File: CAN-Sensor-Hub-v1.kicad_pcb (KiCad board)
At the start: 2 copper layers, 51 x 51.5 mm, 55 parts, among them J1 Conn_01x04, J10 Conn_01x03, J2 Conn_01x04, J3 Conn_01x04, J4 USB_C_Receptacle_USB2.0_14P, J5 Conn_ARM_JTAG_SWD_10, J6 Conn_01x04, J7 Conn_01x04, J8 Conn_01x04, J9 Conn_01x03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

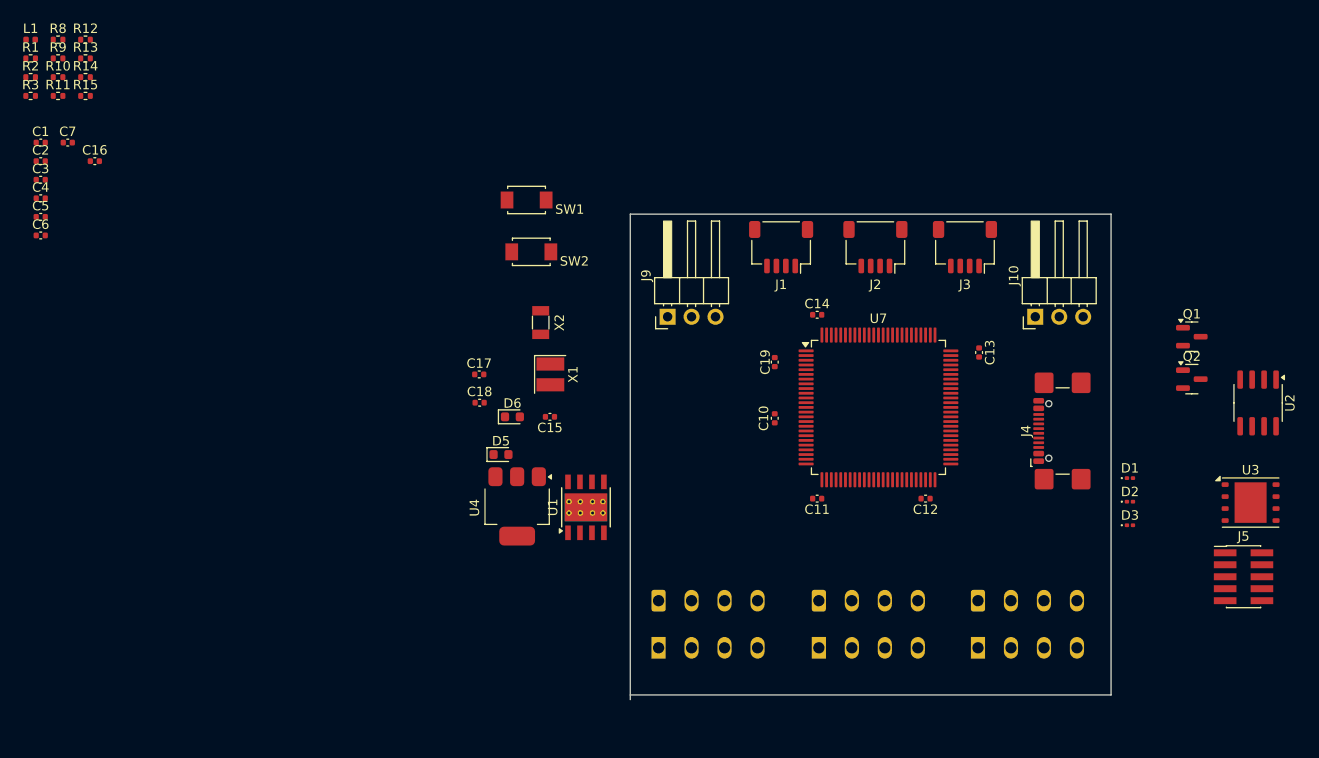
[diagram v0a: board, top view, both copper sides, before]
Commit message: Initial prototype layout done - likely needs to be redone
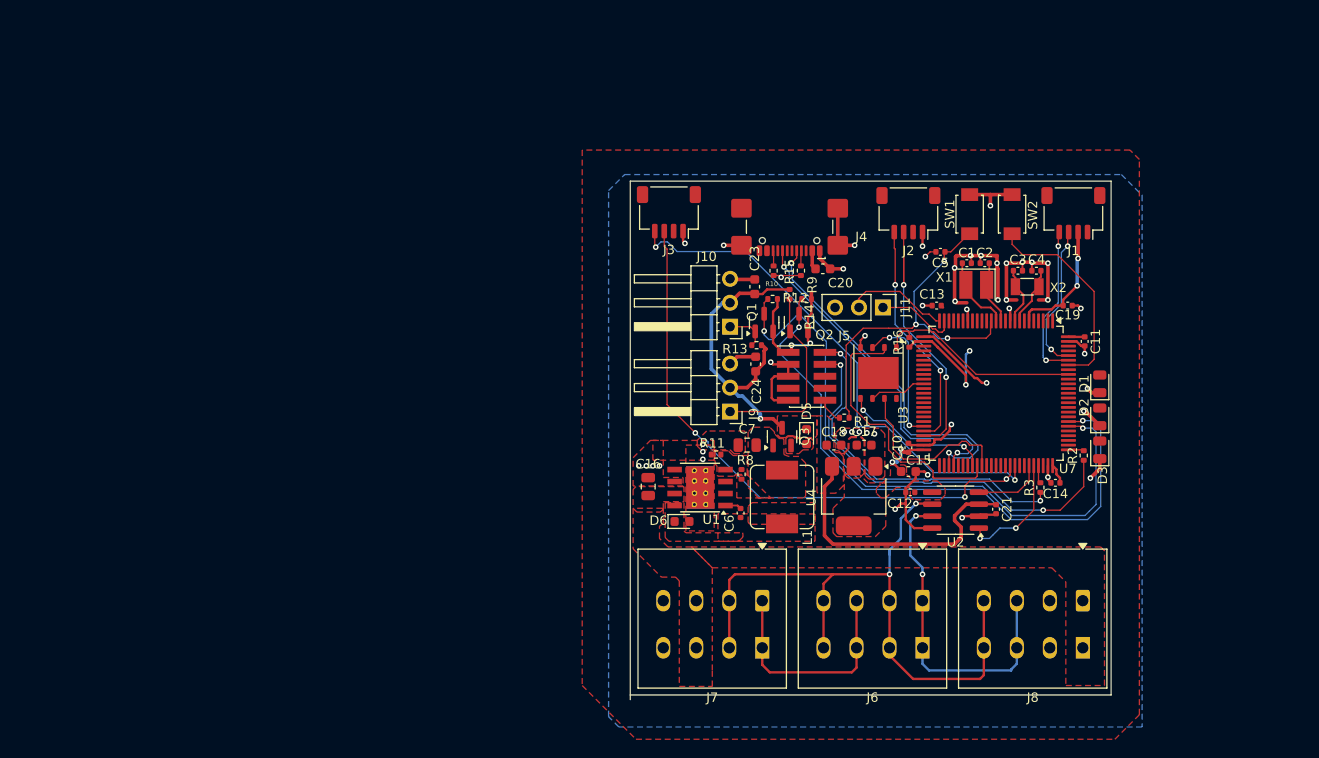
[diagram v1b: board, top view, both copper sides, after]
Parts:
- added C20: 4.7uF, Capacitor_SMD:C_0603_1608Metric, F.Cu at (143.4, 68.3)
- added C21: 100nF, Capacitor_SMD:C_0402_1005Metric, F.Cu at (161.8, 93.8)
- added C23: 10uF, Capacitor_SMD:C_0603_1608Metric, F.Cu at (136.2, 70.2)
- added C24: 10uF, Capacitor_SMD:C_0603_1608Metric, F.Cu at (136.3, 78.4)
- added J11: Conn_01x03, Connector_PinHeader_2.54mm:PinHeader_1x03_P2.54mm_Vertical, F.Cu at (149.8, 72.4)
- added Q3: PMOS, Package_TO_SOT_SMD:SOT-23, F.Cu at (139.1, 86.1)
- added R16: 10k, Resistor_SMD:R_0402_1005Metric, F.Cu at (152.6, 76.1)
- C15, C17, C18: footprint Capacitor_SMD:C_0402_1005Metric -> Capacitor_SMD:C_0603_1608Metric
- C16, C7: footprint Capacitor_SMD:C_0402_1005Metric -> Capacitor_SMD:C_0805_2012Metric
- D1, D2, D3: footprint LED_SMD:LED_0201_0603Metric -> LED_SMD:LED_0805_2012Metric
- J6, J7, J8: moved to F.Cu
- L1: footprint Inductor_SMD:L_0402_1005Metric -> Inductor_SMD:L_Sumida_CDMC6D28_7.25x6.5mm
- moved R2 118.7 mm to (171.1, 88.1), turned to 90 degrees
- moved R3 114.9 mm to (166.5, 91.5), turned to 90 degrees
- moved C4 105.9 mm to (166.1, 68.5), turned to 180 degrees
- moved C3 104.1 mm to (164.1, 68.5)
- moved C2 100.7 mm to (160.6, 67.7)
- moved C1 99.1 mm to (158.7, 67.7), turned to 180 degrees
- moved C5 95.5 mm to (155.9, 66.5), turned to 180 degrees
- moved R1 94.3 mm to (145.7, 84.1)
- moved L1 93.3 mm to (139.1, 92.5), turned to 90 degrees
- moved R8 85.9 mm to (134.8, 90.1), turned to 90 degrees
- moved R9 81.9 mm to (141.1, 68.5), turned to -90 degrees
- moved R14 80.0 mm to (141.7, 71.5), turned to 180 degrees
- moved C6 79.9 mm to (134.7, 94.2), turned to -90 degrees
- moved R11 79.5 mm to (132.1, 88.0), turned to 180 degrees
- moved C7 78.9 mm to (135.4, 87.0), turned to 180 degrees
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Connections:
- C17 pad 2: Net-(U4-GND) -> GNDREF
- C18 pad 2: Net-(U4-GND) -> GNDREF
- C7 pad 1: VDD_5V -> Net-(Q3-D)
- J8 pad 1: CAN_H -> VBAT_12V
- J8 pad 2: CAN_L -> GNDREF
- J8 pad 3: VBAT_12V -> CAN_H
- J8 pad 4: GNDREF -> CAN_L
- L1 pad 2: VDD_5V -> Net-(Q3-D)
- R8 pad 1: VDD_5V -> Net-(Q3-D)
- U4 pad 1: Net-(U4-GND) -> GNDREF
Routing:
- net GNDREF: track 0.00 -> 119.2 mm, vias 0 -> 48
- net CAN_L: track 0.00 -> 72.1 mm, vias 0 -> 2
- net DIO_0_3V3: track 0.00 -> 67.2 mm, vias 0 -> 2
- net DIO_1_3V3: track 0.00 -> 64.2 mm, vias 0 -> 2
- net VDD_5V: track 0.00 -> 63.4 mm, vias 0 -> 1
- net I2C3_SDA: track 0.00 -> 61.9 mm, vias 0 -> 3
- net CAN_H: track 0.00 -> 60.0 mm, vias 0 -> 2
- net I2C3_SCL: track 0.00 -> 55.9 mm, vias 0 -> 2
- net VDD_3V3: track 0.00 -> 51.6 mm, vias 0 -> 8
- net Net-(J5-SWCLK/TCK): track 0.00 -> 44.1 mm, vias 0 -> 2
- net NRST: track 0.00 -> 38.9 mm, vias 0 -> 3
- net OTG_HS_DM: track 0.00 -> 38.0 mm, vias 0 -> 2
- net Net-(J5-SWDIO/TMS): track 0.00 -> 37.4 mm, vias 0 -> 2
- net OTG_HS_DP: track 0.00 -> 36.2 mm, vias 0 -> 2
- net QSPI_IO1: track 0.00 -> 29.2 mm
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- added copper zone on B.Cu, net GNDREF
- added copper zone on F.Cu, net GNDREF
- added copper zone on F.Cu, net Net-(D6-K)
- added copper zone on F.Cu, net Net-(Q3-D)
- added copper zone on F.Cu, net Net-(U1-VSENSE)
- added copper zone on F.Cu, net VBAT_12V
- added copper zone on F.Cu, net VBUS_5V
- added copper zone on F.Cu, net VDD_3V3
- added copper zone on F.Cu, net VDD_5V
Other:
- board size 51 x 51.5 mm -> 51 x 55 mm

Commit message: V0.2 of board, nearly ready for production
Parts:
- removed J7, J8: Conn_01x04, TerminalBlock_WAGO:TerminalBlock_WAGO_2601-1104_1x04_P3.50mm_Horizontal
- removed SW2: BOOT, lib:SW_TS-1088-AR02016
- added C22: 100nF, Capacitor_SMD:C_0402_1005Metric, F.Cu at (156.0, 67.5)
- added C25: 100nF, Capacitor_SMD:C_0402_1005Metric, F.Cu at (152.2, 67.5)
- added C26: 100nF, Capacitor_SMD:C_0402_1005Metric, F.Cu at (145.0, 67.8)
- added C8: 2.2uF, Capacitor_SMD:C_0402_1005Metric, F.Cu at (145.0, 93.0)
- added C9: 2.2uF, Capacitor_SMD:C_0402_1005Metric, F.Cu at (149.2, 78.2)
- added H1: MountingHole, MountingHole:MountingHole_2.7mm_M2.5, F.Cu at (122.2, 63.8)
- added H2: MountingHole, MountingHole:MountingHole_2.7mm_M2.5, F.Cu at (172.7, 81.5)
- added H3: MountingHole, MountingHole:MountingHole_2.7mm_M2.5, F.Cu at (122.1, 110.2)
- added H4: MountingHole, MountingHole:MountingHole_2.7mm_M2.5, F.Cu at (172.7, 110.2)
- added J12: Conn_01x12, TerminalBlock_WAGO:TerminalBlock_WAGO_2601-1112_1x12_P3.50mm_Horizontal, F.Cu at (128.1, 107.7)
- added R4: 160, Resistor_SMD:R_0402_1005Metric, F.Cu at (126.2, 72.2)
- added R5: 60, Resistor_SMD:R_0402_1005Metric, F.Cu at (151.0, 69.7)
- added R6: 160, Resistor_SMD:R_0402_1005Metric, F.Cu at (151.0, 72.6)
- J5: moved to B.Cu
- J6: value Conn_01x04 -> Conn_01x02; footprint TerminalBlock_WAGO:TerminalBlock_WAGO_2601-1104_1x04_P3.50mm_Horizontal -> Connector_PinHeader_2.54mm:PinHeader_1x02_P2.54mm_Vertical
- moved D2 47.6 mm to (127.2, 70.2), turned to 0 degrees
- moved J9 33.5 mm to (164.9, 71.6), turned to 0 degrees
- moved J10 33.5 mm to (164.9, 62.7), turned to 0 degrees
- moved D3 26.7 mm to (153.4, 69.2), turned to 180 degrees
- moved J6 25.7 mm to (165.0, 80.2), turned to 90 degrees
- moved C23 25.2 mm to (161.3, 68.3), turned to 180 degrees
- moved C24 25.1 mm to (161.4, 77.1), turned to 180 degrees
- moved R2 24.6 mm to (148.3, 97.3), turned to 0 degrees
- moved C11 24.2 mm to (159.7, 97.3), turned to 180 degrees
- moved Q1 23.9 mm to (160.9, 70.9), turned to 0 degrees
- moved C19 23.8 mm to (162.7, 95.0)
- moved C4 23.7 mm to (167.2, 92.2), turned to 90 degrees
- moved C17 23.4 mm to (128.9, 73.2), turned to 90 degrees
- moved R13 22.4 mm to (157.8, 69.7), turned to 0 degrees
- moved R1 22.4 mm to (163.8, 97.3)
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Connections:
- D1 pad 2: unconnected-(D1-A-Pad2) -> Net-(D1-A)
- D2 pad 2: unconnected-(D2-A-Pad2) -> Net-(D2-A)
- D3 pad 2: unconnected-(D3-A-Pad2) -> Net-(D3-A)
- J11 pad 1: USART2_TX -> USART2_RX
- J11 pad 2: USART2_RX -> USART2_TX
- J6 pad 1: CAN_H -> GNDREF
- J6 pad 2: CAN_L -> Net-(J6-Pin_2)
- U7 pad 37: unconnected-(U7-PE7-Pad37) -> IO_LED3
- U7 pad 38: unconnected-(U7-PE8-Pad38) -> IO_LED2
- U7 pad 39: unconnected-(U7-PE9-Pad39) -> IO_LED1
- U7 pad 48: unconnected-(U7-VCAP_1-Pad48) -> Net-(U7-VCAP_1)
- U7 pad 73: unconnected-(U7-VCAP_2-Pad73) -> Net-(U7-VCAP_2)
- U7 pad 94: Net-(U7-BOOT0) -> Net-(J6-Pin_2)
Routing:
- net Net-(J5-SWCLK/TCK): track 44.1 -> 8.29 mm, vias 2 -> 1
- net I2C3_SDA: track 61.9 -> 26.8 mm, vias 3 -> 0
- net DIO_1_3V3: track 64.2 -> 33.6 mm
- net DIO_0_3V3: track 67.2 -> 36.7 mm
- net I2C3_SCL: track 55.9 -> 27.2 mm, vias 2 -> 0
- net Net-(J5-SWDIO/TMS): track 37.4 -> 11.3 mm, vias 2 -> 1
- net VBUS_5V: track 2.06 -> 27.3 mm, vias 0 -> 4
- net Net-(J6-Pin_2): track 0.00 -> 22.9 mm, vias 0 -> 3
- net Net-(U7-BOOT0): track 22.1 -> 0.00 mm
- net I2C1_SDA: track 15.8 -> 35.9 mm
- net I2C1_SCL: track 16.7 -> 34.9 mm
- net IO_LED2: track 0.00 -> 15.9 mm, vias 0 -> 2
- net USART2_TX: track 8.70 -> 23.1 mm, vias 0 -> 1
- net QSPI_CLK: track 5.98 -> 19.9 mm, vias 0 -> 2
- net QSPI_IO1: track 29.2 -> 15.3 mm, vias 0 -> 2
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- added copper zone on In1.Cu, net GNDREF
- added copper zone on In2.Cu, net VDD_3V3
- added copper zone on In2.Cu, net VDD_5V
- removed copper zone on B.Cu, net GNDREF
- removed copper zone on F.Cu, net Net-(U1-VSENSE)
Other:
- board size 51 x 55 mm -> 56.8 x 52.6 mm
- copper layers 2 -> 4

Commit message: Production ready board
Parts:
- added C27: 100nF, Capacitor_SMD:C_0402_1005Metric, F.Cu at (163.6, 92.2)
- added R17: 10k, Resistor_SMD:R_0402_1005Metric, F.Cu at (162.6, 95.9)
- added R18: 100k, Resistor_SMD:R_0402_1005Metric, F.Cu at (162.6, 97.5)
- added REF**: LOGO, Graphics_Lib:LOGO, F.Cu at (127.9, 94.0)
- added TP1: TestPoint_Small, TestPoint:TestPoint_Pad_D0.5mm, B.Cu at (149.4, 84.5)
- added TP10: TestPoint_Small, TestPoint:TestPoint_Pad_D0.5mm, F.Cu at (139.8, 74.2)
- added TP11: TestPoint_Small, TestPoint:TestPoint_Pad_D0.5mm, B.Cu at (141.5, 91.1)
- added TP12: TestPoint_Small, TestPoint:TestPoint_Pad_D0.5mm, B.Cu at (143.0, 91.9)
- added TP13: TestPoint_Small, TestPoint:TestPoint_Pad_D0.5mm, B.Cu at (157.8, 68.3)
- added TP14: TestPoint_Small, TestPoint:TestPoint_Pad_D0.5mm, B.Cu at (154.5, 67.9)
- added TP15: TestPoint_Small, TestPoint:TestPoint_Pad_D0.5mm, F.Cu at (148.9, 67.7)
- added TP16: TestPoint_Small, TestPoint:TestPoint_Pad_D0.5mm, F.Cu at (150.2, 68.4)
- added TP17: TestPoint_Small, TestPoint:TestPoint_Pad_D0.5mm, F.Cu at (142.3, 67.4)
- added TP18: TestPoint_Small, TestPoint:TestPoint_Pad_D0.5mm, F.Cu at (141.5, 67.3)
- added TP19: TestPoint_Small, TestPoint:TestPoint_Pad_D0.5mm, B.Cu at (152.5, 78.6)
- added TP2: TestPoint_Small, TestPoint:TestPoint_Pad_D0.5mm, B.Cu at (148.0, 88.5)
- added TP20: TestPoint_Small, TestPoint:TestPoint_Pad_D0.5mm, B.Cu at (149.5, 74.9)
- added TP3: TestPoint_Small, TestPoint:TestPoint_Pad_D0.5mm, B.Cu at (144.2, 85.5)
- added TP4: TestPoint_Small, TestPoint:TestPoint_Pad_D0.5mm, B.Cu at (142.3, 83.3)
- added TP5: TestPoint_Small, TestPoint:TestPoint_Pad_D0.5mm, B.Cu at (141.9, 80.8)
- added TP6: TestPoint_Small, TestPoint:TestPoint_Pad_D0.5mm, B.Cu at (144.5, 86.5)
- added TP7: TestPoint_Small, TestPoint:TestPoint_Pad_D0.5mm, B.Cu at (133.0, 68.8)
- added TP8: TestPoint_Small, TestPoint:TestPoint_Pad_D0.5mm, B.Cu at (132.0, 68.1)
- added TP9: TestPoint_Small, TestPoint:TestPoint_Pad_D0.5mm, F.Cu at (126.2, 76.9)
- C1, C2: value 10pF -> 4.3pF
- C7: footprint Capacitor_SMD:C_0805_2012Metric -> Capacitor_Tantalum_SMD:CP_EIA-3528-21_Kemet-B
- R1, R2, R3: footprint Resistor_SMD:R_0402_1005Metric -> Resistor_SMD:R_0805_2012Metric; moved to B.Cu
- R4: value 160 -> 100
- R5: value 60 -> 100
- R6: value 160 -> 150
- moved J6 16.0 mm to (165.3, 96.2)
- moved R2 7.42 mm to (153.2, 91.7)
- moved R1 6.30 mm to (157.6, 98.1)
- moved R3 5.93 mm to (149.7, 91.7)
- moved J5 3.18 mm to (151.4, 96.5)
- moved C19 2.58 mm to (161.1, 97.0), turned to 90 degrees
- moved C7 1.99 mm to (127.5, 87.0)
- moved C11 1.20 mm to (158.5, 97.5)
- moved C3 0.77 mm to (168.0, 90.2)
- moved C4 0.77 mm to (168.0, 92.2)
- moved X2 0.77 mm to (166.3, 91.2)
- moved H2 0.55 mm to (172.7, 82.0)
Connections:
- J6 pad 1: GNDREF -> Net-(J6-Pin_1)
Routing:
- net QSPI_IO3: track 9.78 -> 21.6 mm
- net QSPI_IO0: track 11.5 -> 22.8 mm
- net SWCLK: track 1.98 -> 12.5 mm, vias 0 -> 1
- net QSPI_IO1: track 15.3 -> 25.9 mm
- net GNDREF: track 112.2 -> 102.2 mm, vias 51 -> 50
- net Net-(J6-Pin_2): track 22.9 -> 14.4 mm, vias 3 -> 0
- net Net-(J5-SWDIO/TMS): track 11.3 -> 2.80 mm, vias 1 -> 0
- net Net-(J5-~{RESET}): track 15.0 -> 7.53 mm, vias 1 -> 0
- net QSPI_IO2: track 17.6 -> 22.8 mm
- net VDD_3V3: track 57.8 -> 62.7 mm, vias 27 -> 26
- net SWDIO/TMS: track 9.44 -> 5.71 mm, vias 2 -> 1
- net CAN_TX: track 2.98 -> 6.26 mm, vias 0 -> 1
- net Net-(J5-SWCLK/TCK): track 8.29 -> 5.27 mm, vias 1 -> 0
- net QSPI_CLK: track 19.9 -> 22.9 mm
- net Net-(J6-Pin_1): track 0.00 -> 2.68 mm
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- added copper zone on B.Cu, net GNDREF
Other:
- outline, holes or cut-outs redrawn
- board text added: "BOOT"
- board text added: "DIO0"
- board text added: "DIO1"
- board text added: "GND"
- board text added: "GND 5V SIG"
- board text added: "RX"
- board text added: "Sensor Hub Board v1 Landon Haugh FRC 2468/2687/2689 (C) 2025"
- board text added: "TX"

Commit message: Made some more adjustments .. USART2 is not compatible with bootloader, changed to USART1
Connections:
- J11 pad 1: USART2_RX -> USART1_RX
- J11 pad 2: USART2_TX -> USART1_TX
- TP19 pad 1: USART2_RX -> USART1_RX
- TP20 pad 1: USART2_TX -> USART1_TX
- U7 pad 24: USART2_TX -> unconnected-(U7-PA2-Pad24)
- U7 pad 25: USART2_RX -> unconnected-(U7-PA3-Pad25)
- U7 pad 68: unconnected-(U7-PA9-Pad68) -> USART1_TX
- U7 pad 69: unconnected-(U7-PA10-Pad69) -> USART1_RX
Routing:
- net USART1_TX: track 0.00 -> 26.8 mm, vias 0 -> 1
- net USART1_RX: track 0.00 -> 25.1 mm, vias 0 -> 1
- net USART2_TX: track 23.1 -> 0.00 mm, vias 1 -> 0
- net USART2_RX: track 21.3 -> 0.00 mm, vias 1 -> 0
- net SWDIO/TMS: track 5.71 -> 6.27 mm
